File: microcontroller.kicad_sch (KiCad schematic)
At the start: 23 parts

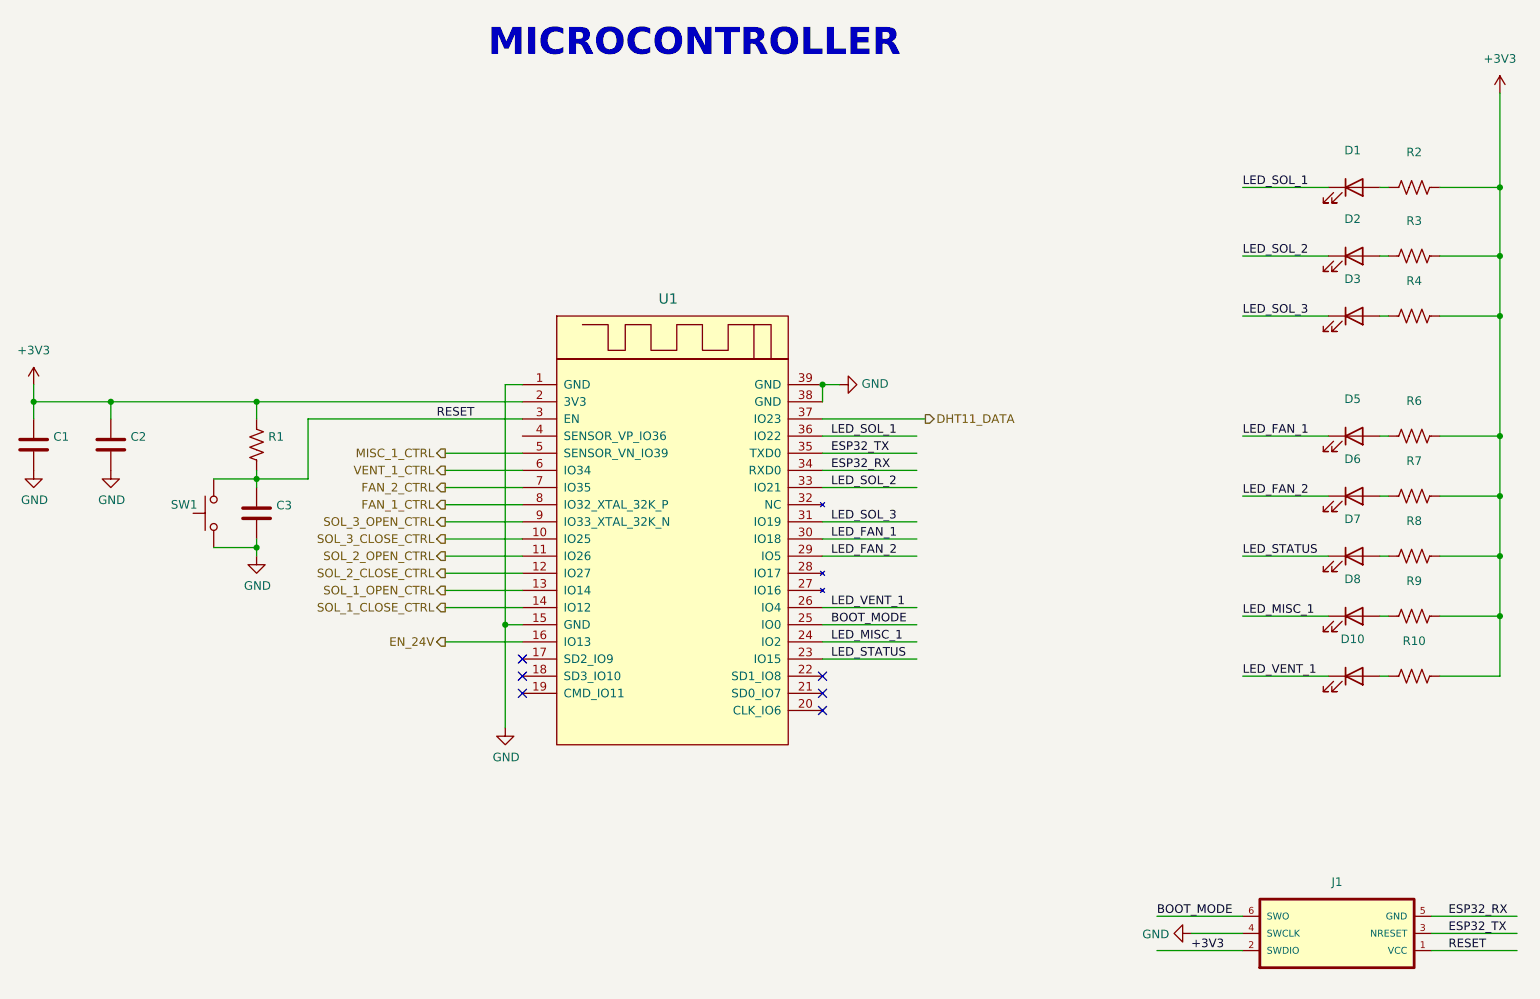
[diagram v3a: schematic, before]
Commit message: Finished initial layout.  Zero DRC errors/warnings.
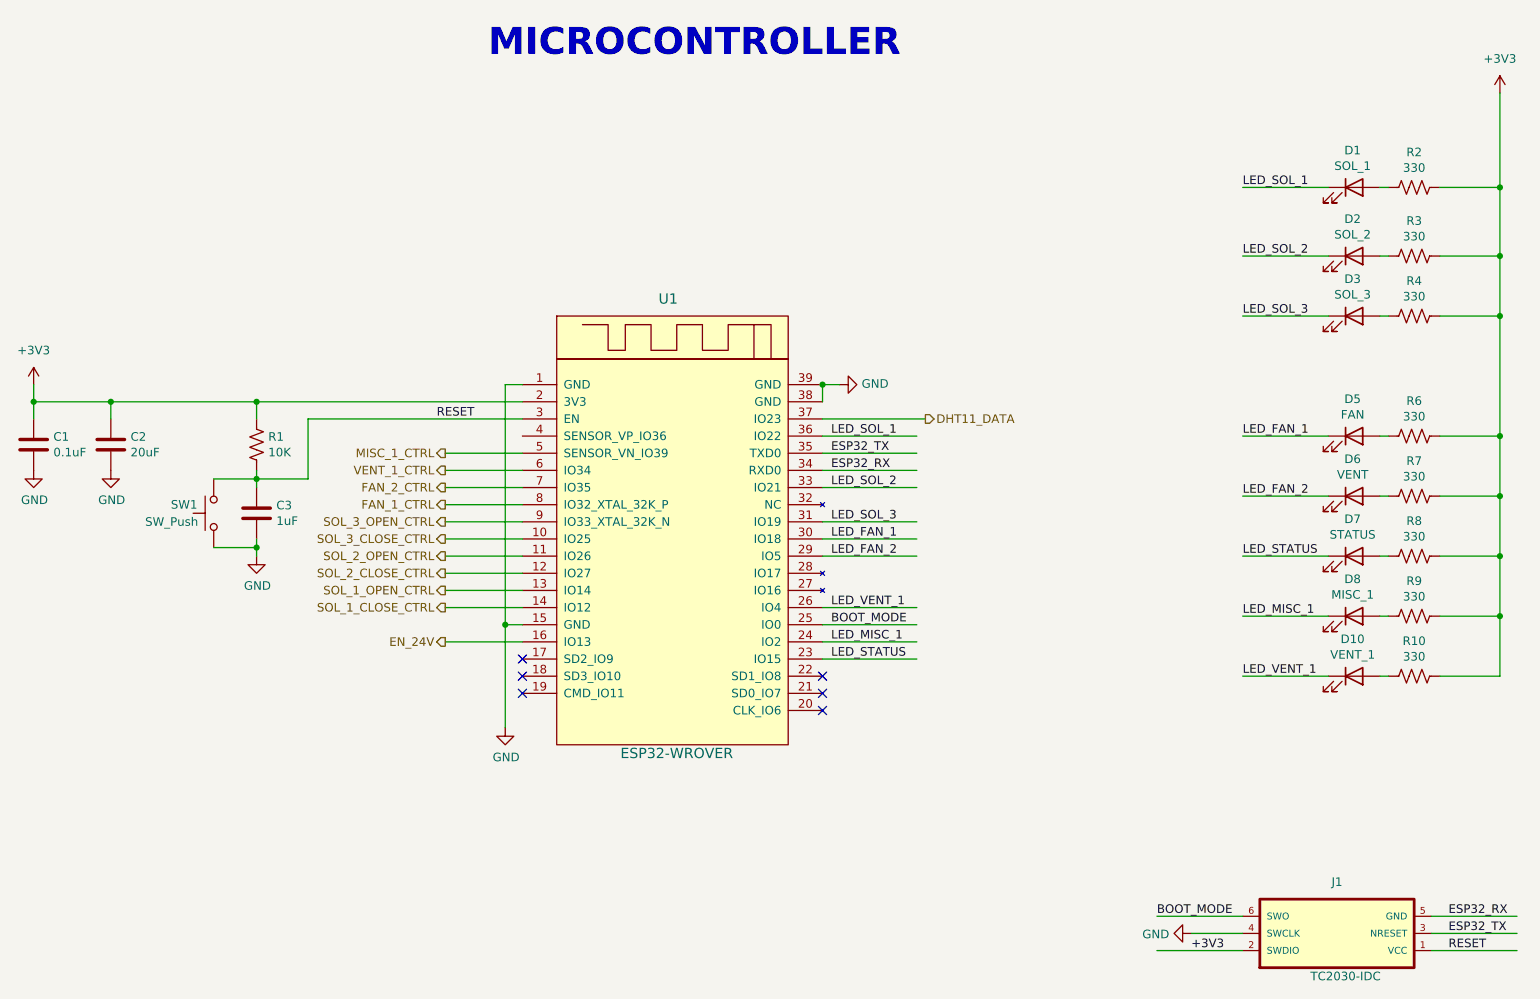
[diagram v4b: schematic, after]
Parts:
- C1: value (none) -> 0.1uF; footprint (none) -> Capacitor_SMD:C_0805_2012Metric
- C2: value (none) -> 20uF; footprint (none) -> Capacitor_SMD:C_0805_2012Metric
- C3: value (none) -> 1uF; footprint (none) -> Capacitor_SMD:C_0805_2012Metric
- D1: value (none) -> SOL_1; footprint (none) -> LED_SMD:LED_0805_2012Metric
- D10: value (none) -> VENT_1; footprint (none) -> LED_SMD:LED_0805_2012Metric
- D2: value (none) -> SOL_2; footprint (none) -> LED_SMD:LED_0805_2012Metric
- D3: value (none) -> SOL_3; footprint (none) -> LED_SMD:LED_0805_2012Metric
- D5: value (none) -> FAN; footprint (none) -> LED_SMD:LED_0805_2012Metric
- D6: value (none) -> VENT; footprint (none) -> LED_SMD:LED_0805_2012Metric
- D7: value (none) -> STATUS; footprint (none) -> LED_SMD:LED_0805_2012Metric
- D8: value (none) -> MISC_1; footprint (none) -> LED_SMD:LED_0805_2012Metric
- J1: value (none) -> TC2030-IDC; footprint (none) -> connector:TC2030-IDC
- R1: value (none) -> 10K; footprint (none) -> Resistor_SMD:R_0805_2012Metric
- R10, R2, R3, R4, R6, R7, R8, R9: value (none) -> 330; footprint (none) -> Resistor_SMD:R_0805_2012Metric
- SW1: value (none) -> SW_Push; footprint (none) -> Button_Switch_SMD:SW_SPST_B3S-1000
- U1: value (none) -> ESP32-WROVER; footprint (none) -> esp32-wrover:ESP32-WROVER
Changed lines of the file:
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@@
       (effects (font (size 1.524 1.524)))
     )
-    (property "Value" "" (id 1) (at 153.67 128.27 0)
+    (property "Value" "ESP32-WROVER" (id 1) (at 153.67 128.27 0)
       (effects (font (size 1.524 1.524)))
     )
-    (property "Footprint" "" (id 2) (at 165.1 100.33 0)
+    (property "Footprint" "esp32-wrover:ESP32-WROVER" (id 2) (at 165.1 100.33 0)
       (effects (font (size 1.524 1.524)) hide)
     )
@@
       (effects (font (size 1.27 1.27)) (justify left))
     )
-    (property "Value" "" (id 1) (at 72.771 83.693 0)
-      (effects (font (size 1.27 1.27)) (justify left))
-    )
-    (property "Footprint" "" (id 2) (at 70.8152 86.36 0)
+    (property "Value" "20uF" (id 1) (at 72.771 83.693 0)
+      (effects (font (size 1.27 1.27)) (justify left))
+    )
+    (property "Footprint" "Capacitor_SMD:C_0805_2012Metric" (id 2) (at 70.8152 86.36 0)
       (effects (font (size 1.27 1.27)) hide)
     )
@@
       (effects (font (size 1.27 1.27)) (justify left))
     )
-    (property "Value" "" (id 1) (at 61.341 83.693 0)
-      (effects (font (size 1.27 1.27)) (justify left))
-    )
-    (property "Footprint" "" (id 2) (at 59.3852 86.36 0)
+    (property "Value" "0.1uF" (id 1) (at 61.341 83.693 0)
+      (effects (font (size 1.27 1.27)) (justify left))
+    )
+    (property "Footprint" "Capacitor_SMD:C_0805_2012Metric" (id 2) (at 59.3852 86.36 0)
       (effects (font (size 1.27 1.27)) hide)
     )
@@
     (in_bom yes) (on_board yes)
     (property "Reference" "D1" (id 0) (at 253.7714 38.9636 0))
-    (property "Value" "" (id 1) (at 253.7714 41.275 0))
-    (property "Footprint" "" (id 2) (at 254 44.45 0)
+    (property "Value" "SOL_1" (id 1) (at 253.7714 41.275 0))
+    (property "Footprint" "LED_SMD:LED_0805_2012Metric" (id 2) (at 254 44.45 0)
       (effects (font (size 1.27 1.27)) hide)
     )
@@
     (in_bom yes) (on_board yes)
     (property "Reference" "D2" (id 0) (at 253.7714 49.1236 0))
-    (property "Value" "" (id 1) (at 253.7714 51.435 0))
-    (property "Footprint" "" (id 2) (at 254 54.61 0)
+    (property "Value" "SOL_2" (id 1) (at 253.7714 51.435 0))
+    (property "Footprint" "LED_SMD:LED_0805_2012Metric" (id 2) (at 254 54.61 0)
       (effects (font (size 1.27 1.27)) hide)
     )
@@
     (in_bom yes) (on_board yes)
     (property "Reference" "D3" (id 0) (at 253.7714 58.0136 0))
-    (property "Value" "" (id 1) (at 253.7714 60.325 0))
-    (property "Footprint" "" (id 2) (at 254 63.5 0)
+    (property "Value" "SOL_3" (id 1) (at 253.7714 60.325 0))
+    (property "Footprint" "LED_SMD:LED_0805_2012Metric" (id 2) (at 254 63.5 0)
       (effects (font (size 1.27 1.27)) hide)
     )
@@
     (in_bom yes) (on_board yes)
     (property "Reference" "D5" (id 0) (at 253.7714 75.7936 0))
-    (property "Value" "" (id 1) (at 253.7714 78.105 0))
-    (property "Footprint" "" (id 2) (at 254 81.28 0)
+    (property "Value" "FAN" (id 1) (at 253.7714 78.105 0))
+    (property "Footprint" "LED_SMD:LED_0805_2012Metric" (id 2) (at 254 81.28 0)
       (effects (font (size 1.27 1.27)) hide)
     )
@@
     (in_bom yes) (on_board yes)
     (property "Reference" "D6" (id 0) (at 253.7714 84.6836 0))
-    (property "Value" "" (id 1) (at 253.7714 86.995 0))
-    (property "Footprint" "" (id 2) (at 254 90.17 0)
+    (property "Value" "VENT" (id 1) (at 253.7714 86.995 0))
+    (property "Footprint" "LED_SMD:LED_0805_2012Metric" (id 2) (at 254 90.17 0)
       (effects (font (size 1.27 1.27)) hide)
     )
@@
     (in_bom yes) (on_board yes)
     (property "Reference" "D7" (id 0) (at 253.7714 93.5736 0))
-    (property "Value" "" (id 1) (at 253.7714 95.885 0))
-    (property "Footprint" "" (id 2) (at 254 99.06 0)
+    (property "Value" "STATUS" (id 1) (at 253.7714 95.885 0))
+    (property "Footprint" "LED_SMD:LED_0805_2012Metric" (id 2) (at 254 99.06 0)
       (effects (font (size 1.27 1.27)) hide)
     )
@@
       (effects (font (size 1.27 1.27)) (justify left))
     )
-    (property "Value" "" (id 1) (at 94.361 93.853 0)
-      (effects (font (size 1.27 1.27)) (justify left))
-    )
-    (property "Footprint" "" (id 2) (at 92.4052 96.52 0)
+    (property "Value" "1uF" (id 1) (at 94.361 93.853 0)
+      (effects (font (size 1.27 1.27)) (justify left))
+    )
+    (property "Footprint" "Capacitor_SMD:C_0805_2012Metric" (id 2) (at 92.4052 96.52 0)
       (effects (font (size 1.27 1.27)) hide)
     )
@@
       (effects (font (size 1.27 1.27)) (justify left))
     )
-    (property "Value" "" (id 1) (at 93.1672 83.693 0)
-      (effects (font (size 1.27 1.27)) (justify left))
-    )
-    (property "Footprint" "" (id 2) (at 92.456 82.804 90)
+    (property "Value" "10K" (id 1) (at 93.1672 83.693 0)
+      (effects (font (size 1.27 1.27)) (justify left))
+    )
+    (property "Footprint" "Resistor_SMD:R_0805_2012Metric" (id 2) (at 92.456 82.804 90)
       (effects (font (size 1.27 1.27)) hide)
     )
@@
     (in_bom yes) (on_board yes)
     (property "Reference" "R2" (id 0) (at 262.89 39.243 90))
-    (property "Value" "" (id 1) (at 262.89 41.5544 90))
-    (property "Footprint" "" (id 2) (at 262.636 45.466 90)
+    (property "Value" "330" (id 1) (at 262.89 41.5544 90))
+    (property "Footprint" "Resistor_SMD:R_0805_2012Metric" (id 2) (at 262.636 45.466 90)
       (effects (font (size 1.27 1.27)) hide)
     )
@@
     (in_bom yes) (on_board yes)
     (property "Reference" "R6" (id 0) (at 262.89 76.073 90))
-    (property "Value" "" (id 1) (at 262.89 78.3844 90))
-    (property "Footprint" "" (id 2) (at 262.636 82.296 90)
+    (property "Value" "330" (id 1) (at 262.89 78.3844 90))
+    (property "Footprint" "Resistor_SMD:R_0805_2012Metric" (id 2) (at 262.636 82.296 90)
       (effects (font (size 1.27 1.27)) hide)
     )
@@
     (in_bom yes) (on_board yes)
     (property "Reference" "R7" (id 0) (at 262.89 84.963 90))
-    (property "Value" "" (id 1) (at 262.89 87.2744 90))
-    (property "Footprint" "" (id 2) (at 262.636 91.186 90)
+    (property "Value" "330" (id 1) (at 262.89 87.2744 90))
+    (property "Footprint" "Resistor_SMD:R_0805_2012Metric" (id 2) (at 262.636 91.186 90)
       (effects (font (size 1.27 1.27)) hide)
     )
@@
     (in_bom yes) (on_board yes)
     (property "Reference" "R8" (id 0) (at 262.89 93.853 90))
-    (property "Value" "" (id 1) (at 262.89 96.1644 90))
-    (property "Footprint" "" (id 2) (at 262.636 100.076 90)
+    (property "Value" "330" (id 1) (at 262.89 96.1644 90))
+    (property "Footprint" "Resistor_SMD:R_0805_2012Metric" (id 2) (at 262.636 100.076 90)
       (effects (font (size 1.27 1.27)) hide)
     )
@@
     (in_bom yes) (on_board yes)
     (property "Reference" "R4" (id 0) (at 262.89 58.293 90))
-    (property "Value" "" (id 1) (at 262.89 60.6044 90))
-    (property "Footprint" "" (id 2) (at 262.636 64.516 90)
+    (property "Value" "330" (id 1) (at 262.89 60.6044 90))
+    (property "Footprint" "Resistor_SMD:R_0805_2012Metric" (id 2) (at 262.636 64.516 90)
       (effects (font (size 1.27 1.27)) hide)
     )
@@
     (in_bom yes) (on_board yes)
     (property "Reference" "R3" (id 0) (at 262.89 49.403 90))
-    (property "Value" "" (id 1) (at 262.89 51.7144 90))
-    (property "Footprint" "" (id 2) (at 262.636 55.626 90)
+    (property "Value" "330" (id 1) (at 262.89 51.7144 90))
+    (property "Footprint" "Resistor_SMD:R_0805_2012Metric" (id 2) (at 262.636 55.626 90)
       (effects (font (size 1.27 1.27)) hide)
     )
@@
     (in_bom yes) (on_board yes)
     (property "Reference" "J1" (id 0) (at 251.46 147.32 0))
-    (property "Value" "" (id 1) (at 252.73 161.29 0))
-    (property "Footprint" "" (id 2) (at 250.19 154.94 0)
+    (property "Value" "TC2030-IDC" (id 1) (at 252.73 161.29 0))
+    (property "Footprint" "connector:TC2030-IDC" (id 2) (at 250.19 154.94 0)
       (effects (font (size 1.27 1.27)) hide)
     )
@@
     (in_bom yes) (on_board yes)
     (property "Reference" "D8" (id 0) (at 253.7714 102.4636 0))
-    (property "Value" "" (id 1) (at 253.7714 104.775 0))
-    (property "Footprint" "" (id 2) (at 254 107.95 0)
+    (property "Value" "MISC_1" (id 1) (at 253.7714 104.775 0))
+    (property "Footprint" "LED_SMD:LED_0805_2012Metric" (id 2) (at 254 107.95 0)
       (effects (font (size 1.27 1.27)) hide)
     )
@@
     (in_bom yes) (on_board yes)
     (property "Reference" "R9" (id 0) (at 262.89 102.743 90))
-    (property "Value" "" (id 1) (at 262.89 105.0544 90))
-    (property "Footprint" "" (id 2) (at 262.636 108.966 90)
+    (property "Value" "330" (id 1) (at 262.89 105.0544 90))
+    (property "Footprint" "Resistor_SMD:R_0805_2012Metric" (id 2) (at 262.636 108.966 90)
       (effects (font (size 1.27 1.27)) hide)
     )
@@
     (in_bom yes) (on_board yes)
     (property "Reference" "D10" (id 0) (at 253.7714 111.3536 0))
-    (property "Value" "" (id 1) (at 253.7714 113.665 0))
-    (property "Footprint" "" (id 2) (at 254 116.84 0)
+    (property "Value" "VENT_1" (id 1) (at 253.7714 113.665 0))
+    (property "Footprint" "LED_SMD:LED_0805_2012Metric" (id 2) (at 254 116.84 0)
       (effects (font (size 1.27 1.27)) hide)
     )
@@
     (in_bom yes) (on_board yes)
     (property "Reference" "R10" (id 0) (at 262.89 111.633 90))
-    (property "Value" "" (id 1) (at 262.89 113.9444 90))
-    (property "Footprint" "" (id 2) (at 262.636 117.856 90)
+    (property "Value" "330" (id 1) (at 262.89 113.9444 90))
+    (property "Footprint" "Resistor_SMD:R_0805_2012Metric" (id 2) (at 262.636 117.856 90)
       (effects (font (size 1.27 1.27)) hide)
     )
@@
       (effects (font (size 1.27 1.27)) (justify right))
     )
-    (property "Value" "" (id 1) (at 74.93 93.98 90)
+    (property "Value" "SW_Push" (id 1) (at 74.93 93.98 90)
       (effects (font (size 1.27 1.27)) (justify right))
     )
-    (property "Footprint" "" (id 2) (at 80.01 92.71 0)
-      (effects (font (size 1.27 1.27)) hide)
-    )
+    (property "Footprint" "Button_Switch_SMD:SW_SPST_B3S-1000" (id 2) (at 80.01 92.71 0)
+      (effects (font (size 1.27 1.27)) hide)
+    )
